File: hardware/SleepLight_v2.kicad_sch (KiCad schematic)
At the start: 71 parts, among them J2 UJ20-C-H-C-1-SMT-TR, Q1 ERT-J1VG103FM, U1 ESP32-C3-WROOM-02-N4, U2 TLV73333PDBVR, U3 MCP73871-1AAI/ML, U4 TPS61222DCKT, U6 SN74AHCT1G125DBVR

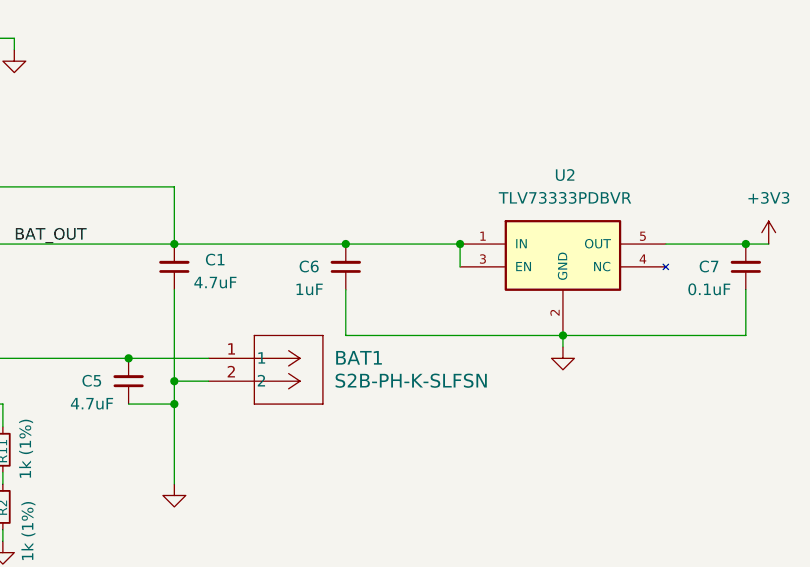
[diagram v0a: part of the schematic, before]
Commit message: fix: ldo en pull-up resistor
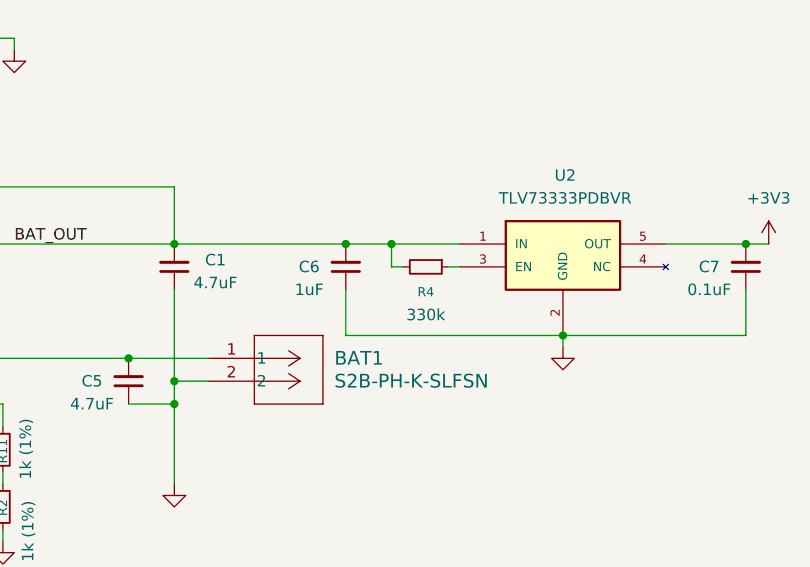
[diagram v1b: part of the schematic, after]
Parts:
- added R4: 330k, Resistor_SMD:R_0603_1608Metric, symbol Device:R_Small
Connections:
- net BAT_OUT: now also R4.2; no longer U2.3 (EN)
- new net: R4.1, U2.3 (EN)
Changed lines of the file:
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@@
 	)
 	(junction
+		(at 140.97 137.16)
+		(diameter 0)
+		(color 0 0 0 0)
+	)
+	(junction
 		(at 271.78 213.36)
 		(diameter 0)
@@
 	)
 	(junction
-		(at 148.59 137.16)
-		(diameter 0)
-		(color 0 0 0 0)
-	)
-	(junction
 		(at 318.77 215.9)
 		(diameter 0)
@@
 	(wire
 		(pts
+			(xy 142.24 139.7) (xy 140.97 139.7)
+		)
+		(stroke
+			(width 0)
+			(type default)
+		)
+	)
+	(wire
+		(pts
 			(xy 271.78 106.68) (xy 281.94 106.68)
 		)
@@
 	(wire
 		(pts
+			(xy 140.97 137.16) (xy 148.59 137.16)
+		)
+		(stroke
+			(width 0)
+			(type default)
+		)
+	)
+	(wire
+		(pts
 			(xy 271.78 185.42) (xy 318.77 185.42)
 		)
@@
 	(wire
 		(pts
-			(xy 148.59 137.16) (xy 148.59 139.7)
-		)
-		(stroke
-			(width 0)
-			(type default)
-		)
-	)
-	(wire
-		(pts
 			(xy 271.78 203.2) (xy 318.77 203.2)
 		)
@@
 	(wire
 		(pts
-			(xy 135.89 137.16) (xy 148.59 137.16)
+			(xy 135.89 137.16) (xy 140.97 137.16)
 		)
 		(stroke
@@
 	(wire
 		(pts
+			(xy 147.32 139.7) (xy 148.59 139.7)
+		)
+		(stroke
+			(width 0)
+			(type default)
+		)
+	)
+	(wire
+		(pts
 			(xy 271.78 142.24) (xy 281.94 142.24)
 		)
@@
 	(wire
 		(pts
+			(xy 140.97 139.7) (xy 140.97 137.16)
+		)
+		(stroke
+			(width 0)
+			(type default)
+		)
+	)
+	(wire
+		(pts
 			(xy 88.9 157.48) (xy 92.71 157.48)
 		)
@@
 					(unit 1)
 				)
+			)
+		)
+	)
+	(symbol
+		(lib_id "Device:R_Small")
+		(at 144.78 139.7 270)
+		(unit 1)
+		(exclude_from_sim no)
+		(in_bom yes)
+		(on_board yes)
+		(dnp no)
+		(property "Reference" "R4"
+			(at 144.78 142.494 90)
+			(effects
+				(font
+					(size 1.016 1.016)
+				)
+			)
+		)
+		(property "Value" "330k"
+			(at 144.78 145.034 90)
+			(effects
+				(font
+					(size 1.27 1.27)
+				)
+			)
+		)
+		(property "Footprint" "Resistor_SMD:R_0603_1608Metric"
+			(at 144.78 139.7 0)
+			(effects
+				(font
+					(size 1.27 1.27)
+				)
+				(hide yes)
+			)
+		)
+		(property "Datasheet" "~"
+			(at 144.78 139.7 0)
+			(effects
+				(font
+					(size 1.27 1.27)
+				)
+				(hide yes)
+			)
+		)
+		(property "Description" "Resistor, small symbol"
+			(at 144.78 139.7 0)
+			(effects
+				(font
+					(size 1.27 1.27)
+				)
+				(hide yes)
+			)
+		)
+		(pin "1"
+		)
+		(pin "2"
+		)
+		(instances
+			(project "SleepLight_v2"
+				(path "/b3e37ba4-2584-4b8f-982e-8497657a80ab"
+					(reference "R4")
+					(unit 1)
+				)
